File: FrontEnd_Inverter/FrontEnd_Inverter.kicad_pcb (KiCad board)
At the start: 4 copper layers, 210 x 127 mm, 108 parts, among them J1 GateDriverConn, J2 GateDriverConn, J200 AuxConnector_Analog, J201 DigOut_Connector, J3 GateDriverConn, P1 CONN_01X03, P10 CONN_01X02, P2 CONN_01X03, T1 SKiiP_13ACM12V18, U100 ACS720KLATR-35B, U200 ACS720KLATR-35B, U30 ISE0505A-H, U300 ACS720KLATR-35B, U40 ACPL-C87B, U400 ACS720KLATR-35B, U50 ACPL-C87B, U500 ACS720KLATR-35B

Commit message: further adjustments to pcb layout.
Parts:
- added P20: CONN_01X02, Connector_Phoenix_GMSTB:PhoenixContact_GMSTBA_2,5_3-G-7,62_1x03_P7.62mm_Horizontal, F.Cu at (42.9, 125.9)
- moved D21 47.6 mm to (216.1, 124.7)
- moved R21 47.6 mm to (214.6, 129.3)
- moved TP22 47.6 mm to (205.8, 114.7)
- moved TP21 47.6 mm to (197.8, 115.8)
- moved P10 25.2 mm to (48.8, 55.8)
- moved P1 13.3 mm to (48.7, 31.3)
- moved C500 2.26 mm to (89.0, 30.4)
- moved C503 2.26 mm to (88.8, 35.6)
- moved R501 2.26 mm to (94.0, 28.1)
- moved R502 2.26 mm to (94.0, 31.8)
- moved C501 2.26 mm to (93.9, 34.2)
- moved C502 2.26 mm to (85.1, 34.2)
- moved R503 2.26 mm to (85.1, 28.1)
- moved R504 2.26 mm to (85.1, 31.8)
- moved U400 2.26 mm to (88.3, 42.2)
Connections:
- T1 pad 7: DC+ -> +VDC
- T1 pad 8: DC+ -> +VDC
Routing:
- net DC-_out: track 270.5 -> 249.2 mm, vias 5 -> 4
- net T+: track 0.00 -> 21.3 mm, vias 0 -> 1
- net Net-(D1-Pad15): track 88.3 -> 93.7 mm
- net Net-(D1-Pad1): track 76.6 -> 82.1 mm
- net Net-(D1-Pad18): track 69.7 -> 75.2 mm
- net I+: track 3.03 -> 0.00 mm
- added copper zone on F.Cu, net +VDC
- added copper zone on F.Cu, net DC+_in
- added copper zone on F.Cu, net Net-(D1-Pad14)
- removed copper zone on F.Cu, net (none)
- removed copper zone on F.Cu, net DC+

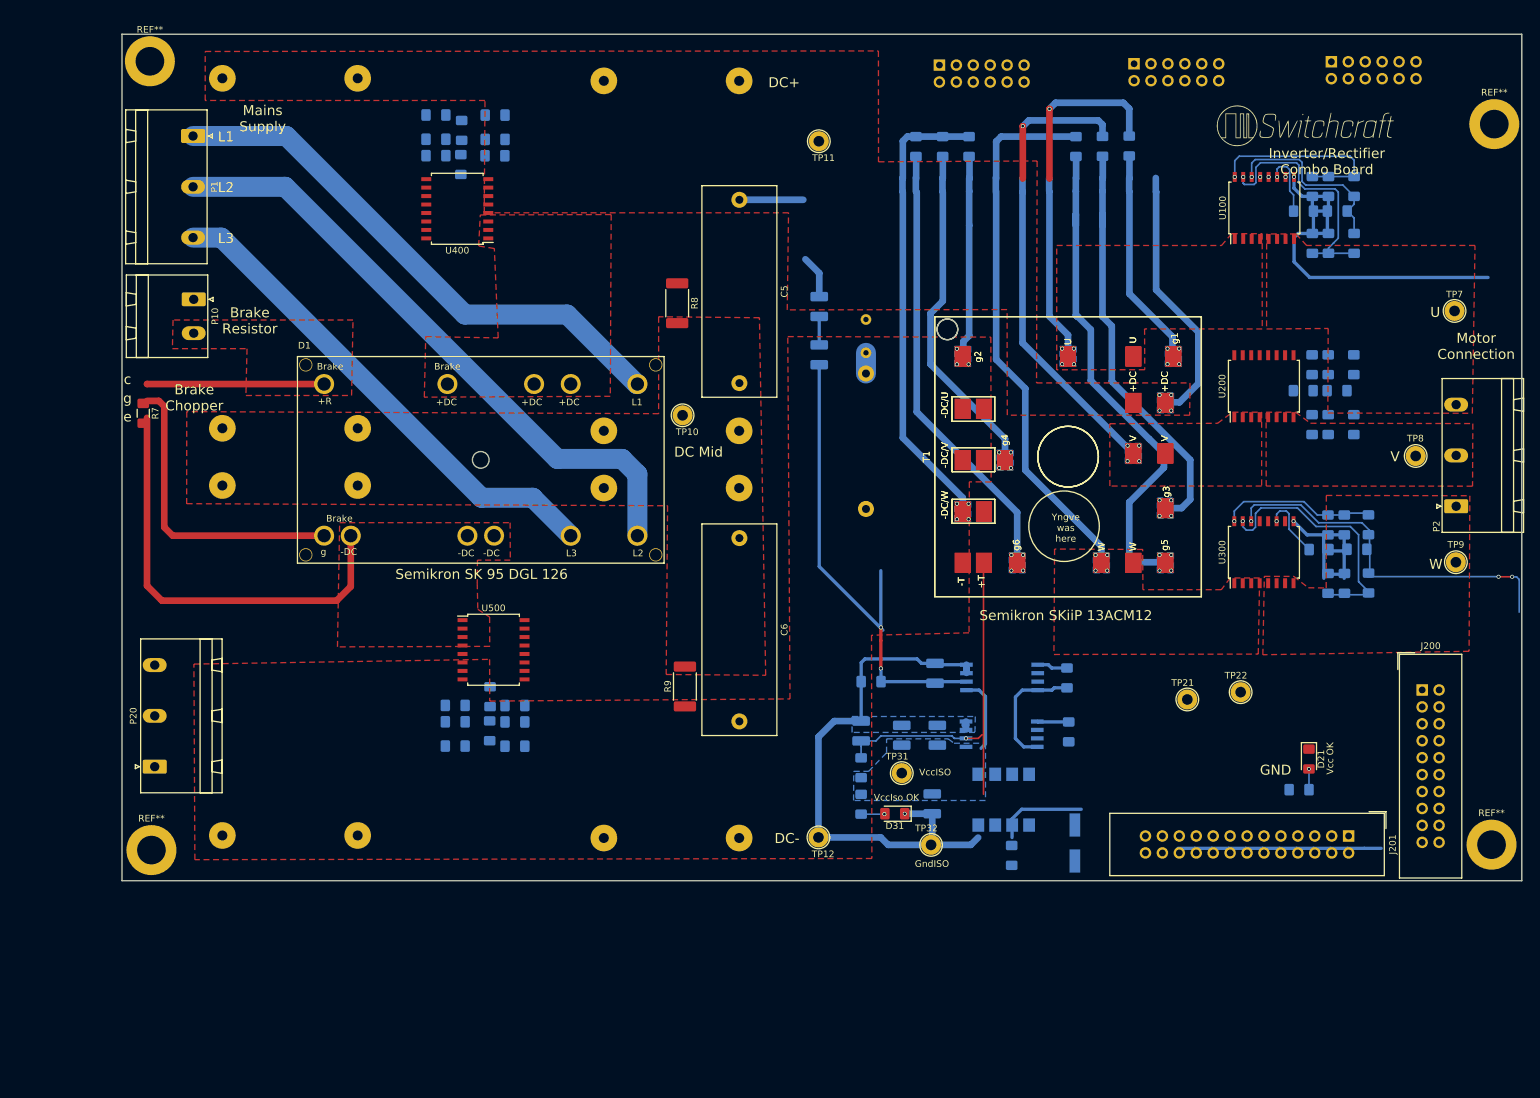
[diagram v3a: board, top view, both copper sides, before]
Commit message: Updated connector type for brake chopper gatedriver connection from GMSTBA to 2.54mm pin header.  More work with tracks and zones on PCB layout.
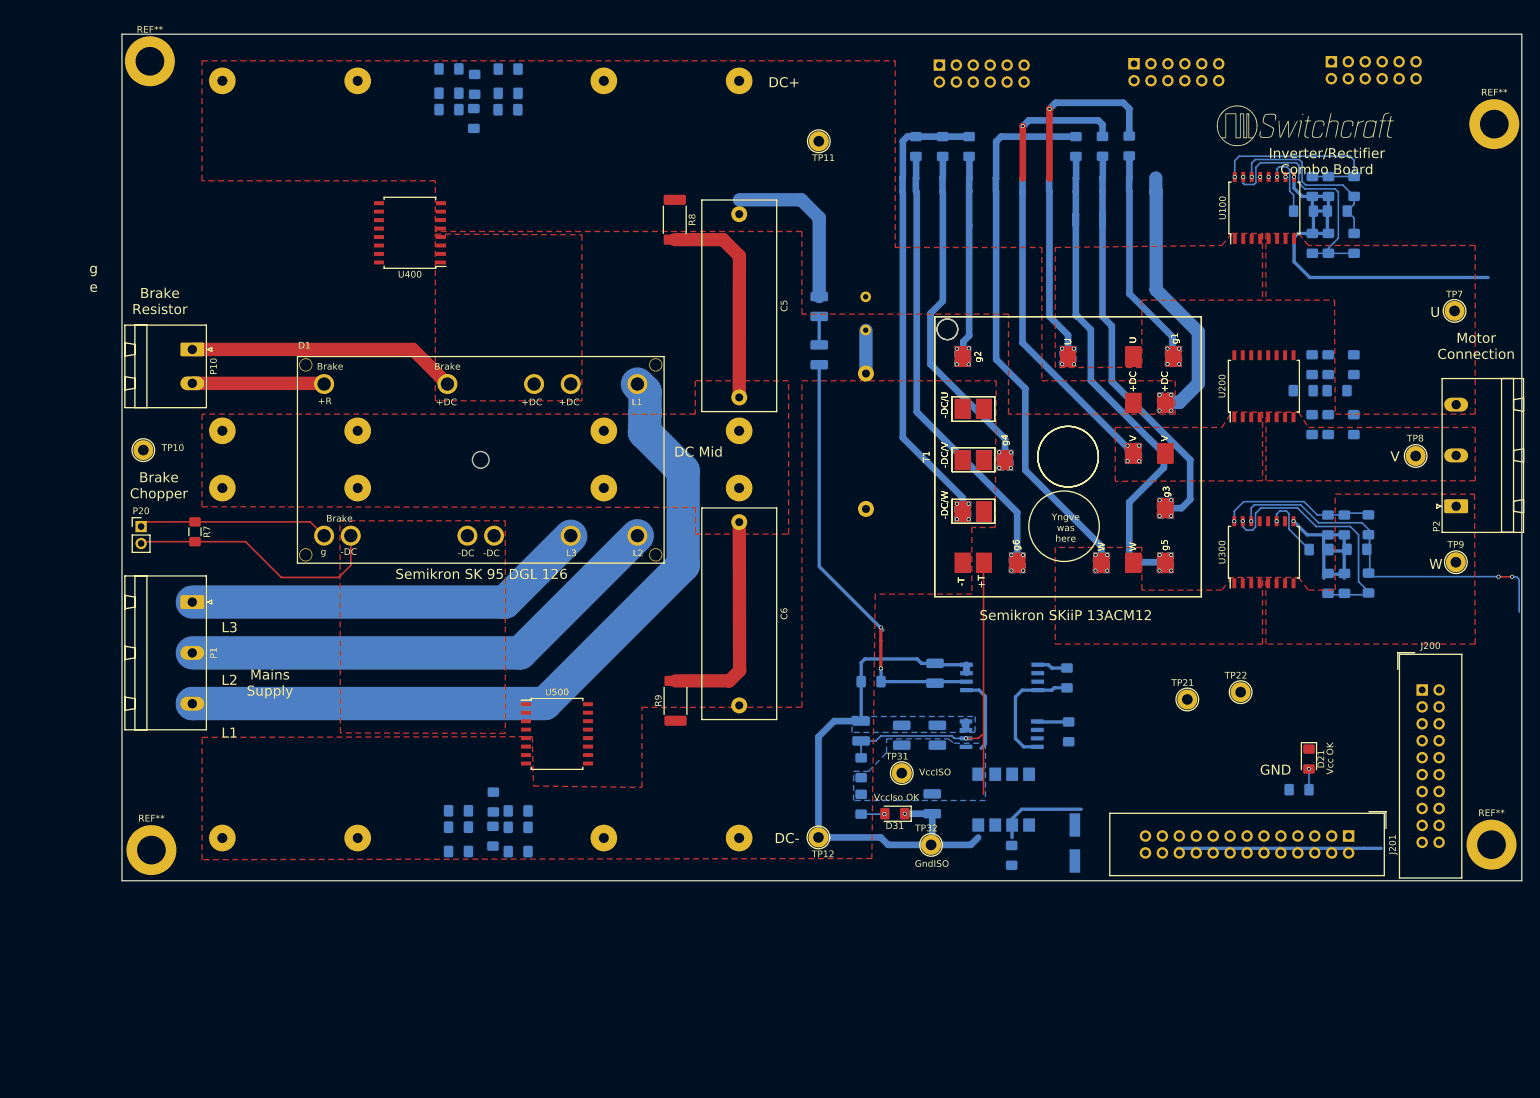
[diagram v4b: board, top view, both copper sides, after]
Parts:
- P20: footprint Connector_Phoenix_GMSTB:PhoenixContact_GMSTBA_2,5_3-G-7,62_1x03_P7.62mm_Horizontal -> Connector_PinHeader_2.54mm:PinHeader_1x02_P2.54mm_Vertical
- moved TP10 81.1 mm to (41.2, 78.4)
- moved P1 69.9 mm to (48.5, 101.2)
- moved P20 36.1 mm to (40.9, 89.9), turned to 0 degrees
- moved R7 19.4 mm to (49.0, 90.7)
- moved R403 15.8 mm to (97.4, 138.6)
- moved C400 15.8 mm to (93.6, 136.3)
- moved C403 15.8 mm to (93.7, 131.2)
- moved C401 15.8 mm to (88.5, 132.5)
- moved R401 15.8 mm to (88.5, 138.6)
- moved C402 15.8 mm to (97.4, 132.5)
- moved R404 15.8 mm to (97.4, 135.0)
- moved R402 15.8 mm to (88.5, 135.0)
- moved U500 15.8 mm to (103.3, 121.0)
- moved R8 12.5 mm to (120.9, 43.8)
- moved U400 7.96 mm to (81.2, 45.8)
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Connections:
- P1 pad 1: Net-(D1-Pad1) -> Net-(D1-Pad18)
- P1 pad 3: Net-(D1-Pad18) -> Net-(D1-Pad1)
- T1 pad 10: DC-_out -> T-
- T1 pad 11: DC-_out -> T-
- T1 pad 12: DC-_out -> T-
- T1 pad 13: DC-_out -> T-
- T1 pad 14: DC-_out -> T-
- T1 pad 21: DC-_out -> T+
- T1 pad 22: DC-_out -> T-
- T1 pad 7: DC+ -> +VDC
- T1 pad 8: DC+ -> +VDC
- T1 pad 9: DC-_out -> T-
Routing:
- net Net-(C1-Pad2): track 0.00 -> 63.7 mm
- net +VDC: track 16.1 -> 64.3 mm, vias 0 -> 4
- net DC+_in: track 0.00 -> 40.4 mm
- net DC+: track 39.3 -> 0.00 mm, vias 4 -> 0
- net DC-_out: track 249.2 -> 214.5 mm, vias 4 -> 0
- net T+: track 21.3 -> 56.1 mm
- net Net-(D1-Pad1): track 82.1 -> 112.3 mm
- net DC-_in: track 65.2 -> 39.0 mm
- net Net-(D1-Pad15): track 93.7 -> 74.1 mm
- net BC_gate: track 45.6 -> 28.6 mm
- net Net-(D1-Pad18): track 75.2 -> 60.9 mm
- net Net-(C51-Pad1): track 73.5 -> 64.9 mm
- net Net-(D1-Pad14): track 26.6 -> 19.8 mm
- net Net-(C7-Pad2): track 3.10 -> 6.53 mm
- net T2_g: vias 4 -> 5
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- removed copper zone on F.Cu, net Net-(D1-Pad14)
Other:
- board text removed: "c"
